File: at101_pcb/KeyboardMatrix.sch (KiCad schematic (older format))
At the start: 229 parts, among them SW1.1 KEY_ESCAPE, SW1.10 KEY_F9, SW1.11 KEY_F10, SW1.12 KEY_F11, SW1.13 KEY_F12, SW1.14 KEY_PRINTSCREEN, SW1.15 KEY_SCROLL_LOCK, SW1.16 KEY_PAUSE, SW1.2 KEY_F1, SW1.3 KEY_F2, SW1.4 KEY_F3, SW1.5 KEY_F4, SW1.6 KEY_F5, SW1.7 KEY_F6, SW1.8 KEY_F7, SW1.9 KEY_F8, SW2.1 KEY_BACKQUOTE, SW2.10 KEY_9, SW2.11 KEY_0, SW2.12 KEY_MINUS, SW2.13 KEY_EQUALS, SW2.14 KEY_BACKSPACE, SW2.15 KEY_INSERT, SW2.16 KEY_HOME, SW2.17 KEY_PGUP, SW2.18 KEY_NUMLOCK, SW2.19 KEY_NUMDIVIDE, SW2.2 KEY_1, SW2.20 KEY_NUMTIMES, SW2.21 KEY_NUMMINUS, SW2.3 KEY_2, SW2.4 KEY_3, SW2.5 KEY_4, SW2.6 KEY_5, SW2.7 KEY_6, SW2.8 KEY_7, SW2.9 KEY_8, SW3.1 KEY_TAB, SW3.10 KEY_O, SW3.11 KEY_P, SW3.12 KEY_LEFTBRACKET, SW3.13 KEY_RIGHTBRACKET, SW3.14 KEY_ANSIBACKSLASH, SW3.15 KEY_DELETE, SW3.16 KEY_END, SW3.17 KEY_PGDN, SW3.18 KEY_NUM7, SW3.19 KEY_NUM8, SW3.2 KEY_Q, SW3.20 KEY_NUM9, SW3.21 KEY_NUMPLUS, SW3.3 KEY_W, SW3.4 KEY_E, SW3.5 KEY_R, SW3.6 KEY_T, SW3.7 KEY_Y, SW3.8 KEY_U, SW3.9 KEY_I, SW3B.1 KEY_NUMBIGPLUS, SW4.1 KEY_CAPSLOCK, SW4.10 KEY_L, SW4.11 KEY_SEMICOLON, SW4.12 KEY_QUOTE, SW4.13 KEY_ISOBACKSLASH, SW4.14 KEY_ISOENTER, SW4.15 KEY_ENTER, SW4.16 KEY_NUM4, SW4.17 KEY_NUM5, SW4.18 KEY_NUM6, SW4.19 KEY_NUMEQUALS, SW4.2 KEY_A, SW4.3 KEY_S, SW4.4 KEY_D, SW4.5 KEY_F, SW4.6 KEY_G, SW4.7 KEY_H, SW4.8 KEY_J, SW4.9 KEY_K, SW4.B1 KEY_CAPSLOCK_1.5, SW4C.1 KEY_CAPSLOCK_1.25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

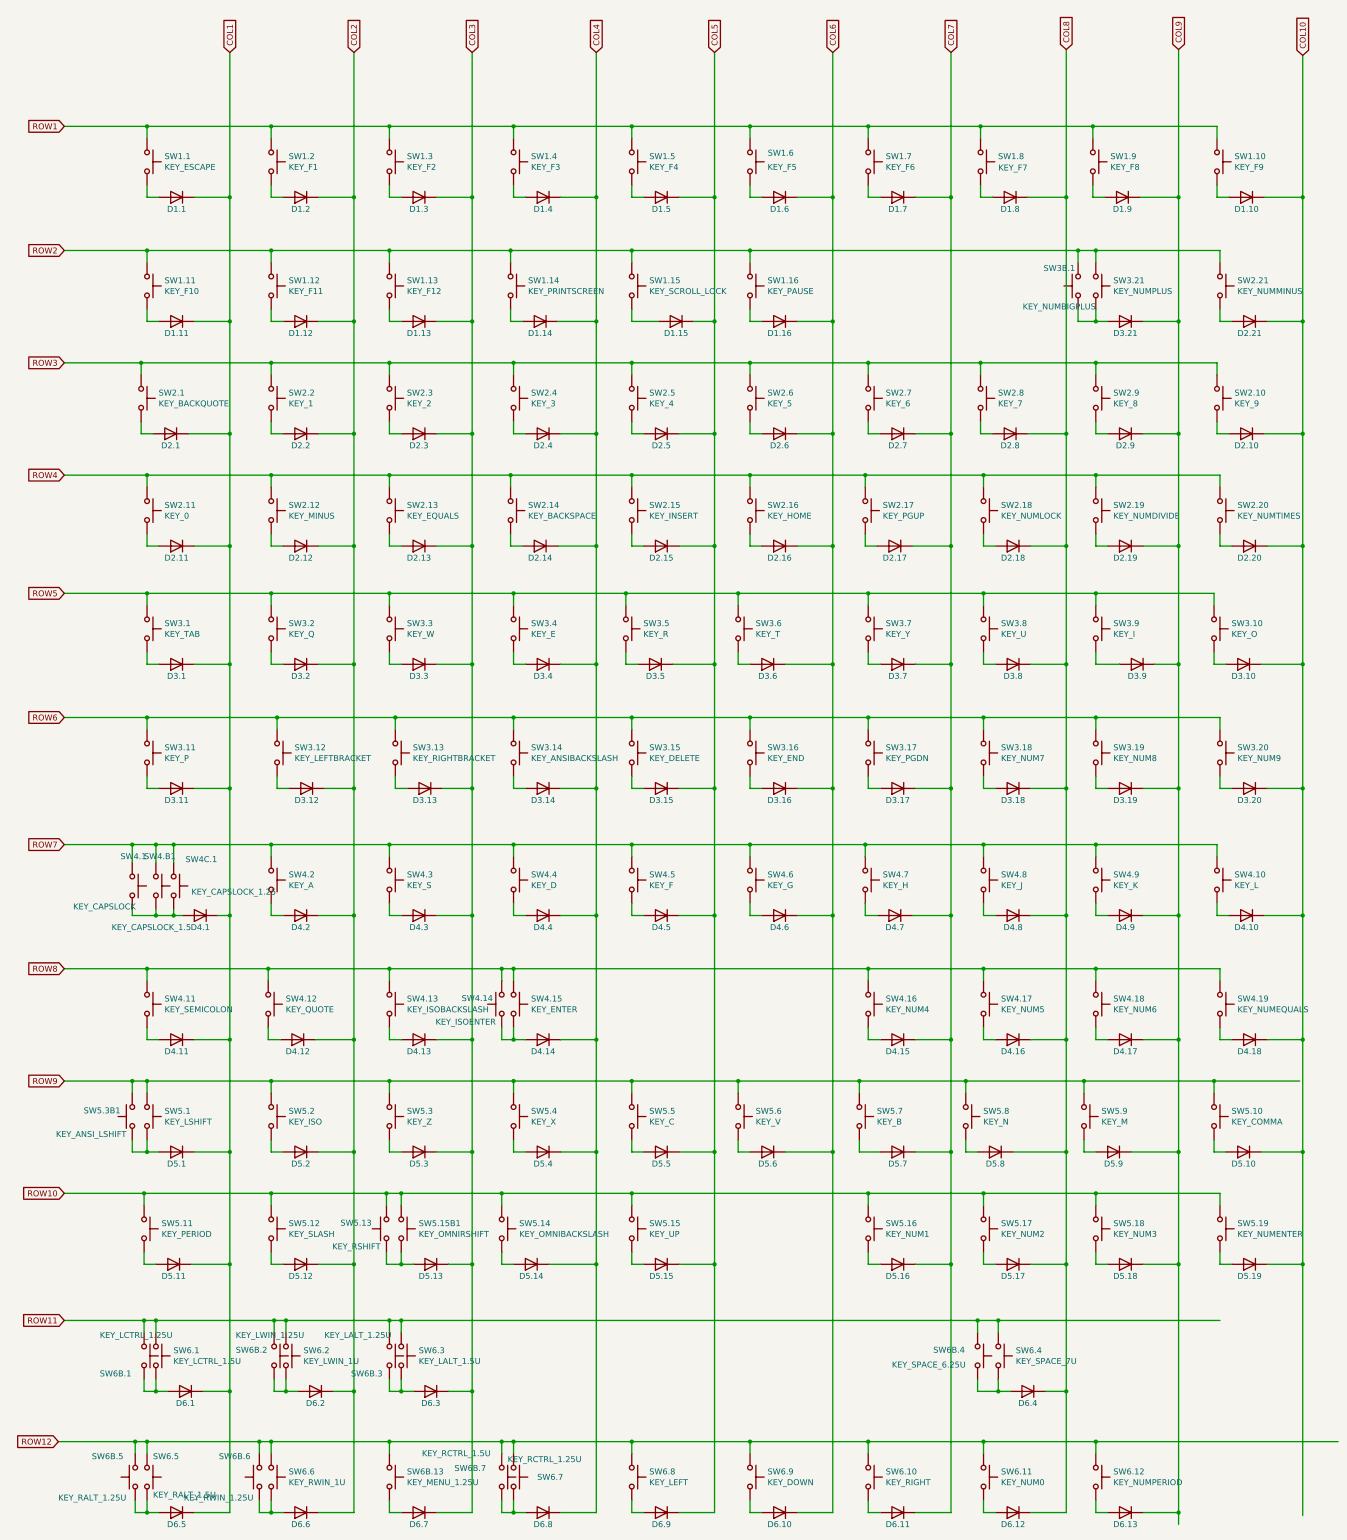
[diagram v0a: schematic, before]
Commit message: Correct AT10[12]W? switch labels
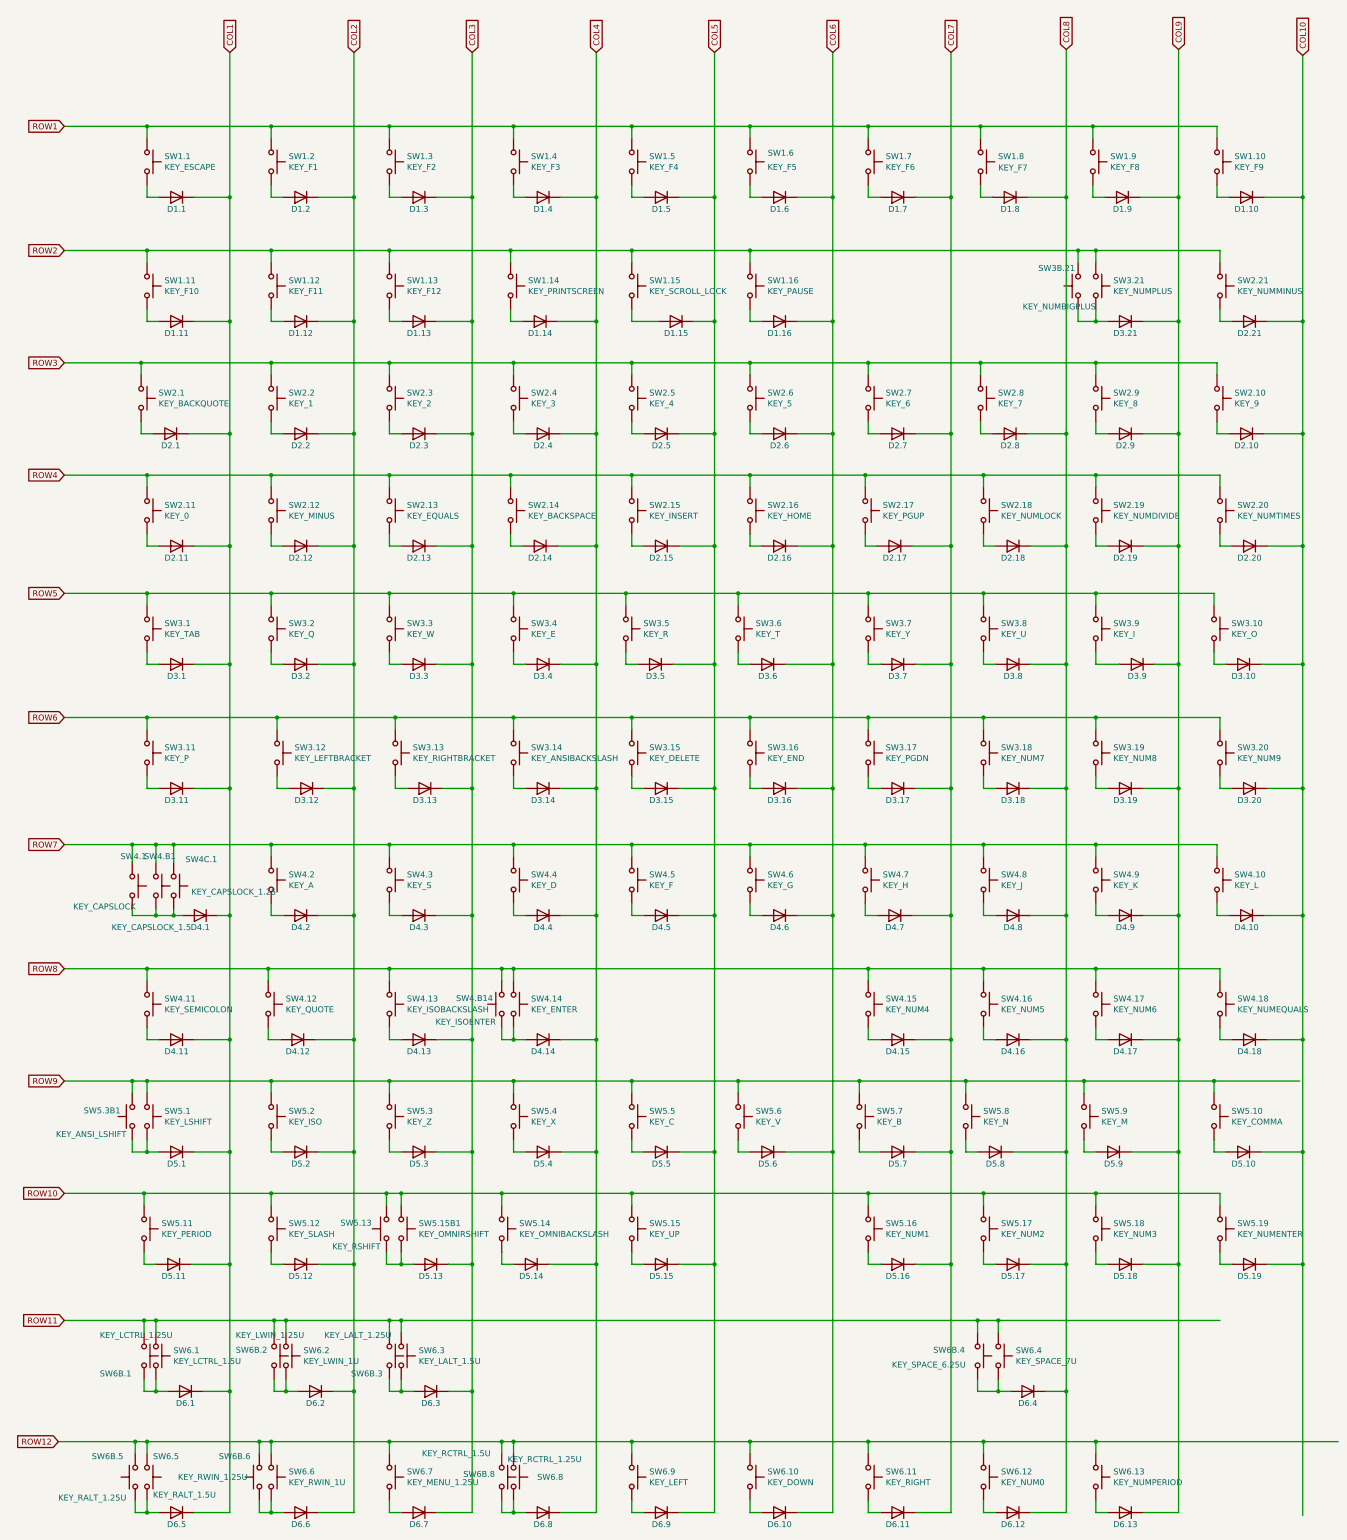
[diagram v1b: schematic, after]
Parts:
- renumbered SW3B.1 to SW3B.21, SW4.15 to SW4.14, SW4.16 to SW4.15, SW4.17 to SW4.16, SW4.18 to SW4.17, SW4.19 to SW4.18, SW4.14 to SW4.B14, SW6.9 to SW6.10, SW6.10 to SW6.11, SW6.11 to SW6.12, SW6.12 to SW6.13, SW6B.13 to SW6.7, SW6.7 to SW6.8, SW6.8 to SW6.9, SW6B.7 to SW6B.8
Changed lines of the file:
@@
 	17075 10350 17275 10350
 $Comp
-L Switch:SW_Push SW4.16
+L Switch:SW_Push SW4.15
 U 1 1 5D151639
 P 15150 13225
-F 0 "SW4.16" V 15104 13373 50  0000 L CNN
+F 0 "SW4.15" V 15104 13373 50  0000 L CNN
 F 1 "KEY_NUM4" V 15195 13373 50  0000 L CNN
 F 2 "MX_Alps_Hybrid:MX-1U-NoLED" H 15150 13425 50  0001 C CNN
@@
 	10100 11975 10100 11875
 $Comp
-L Switch:SW_Push SW4.17
+L Switch:SW_Push SW4.16
 U 1 1 5D151718
 P 16125 13225
-F 0 "SW4.17" V 16079 13373 50  0000 L CNN
+F 0 "SW4.16" V 16079 13373 50  0000 L CNN
 F 1 "KEY_NUM5" V 16170 13373 50  0000 L CNN
 F 2 "MX_Alps_Hybrid:MX-1U-NoLED" H 16125 13425 50  0001 C CNN
@@
 	11100 11975 11100 11875
 $Comp
-L Switch:SW_Push SW4.18
+L Switch:SW_Push SW4.17
 U 1 1 5D1517E5
 P 17075 13225
-F 0 "SW4.18" V 17029 13373 50  0000 L CNN
+F 0 "SW4.17" V 17029 13373 50  0000 L CNN
 F 1 "KEY_NUM6" V 17120 13373 50  0000 L CNN
 F 2 "MX_Alps_Hybrid:MX-1U-NoLED" H 17075 13425 50  0001 C CNN
@@
 	14150 8400 14250 8400
 $Comp
-L Switch:SW_Push SW4.15
+L Switch:SW_Push SW4.14
 U 1 1 5D151A5B
 P 12150 13225
-F 0 "SW4.15" V 12104 13373 50  0000 L CNN
+F 0 "SW4.14" V 12104 13373 50  0000 L CNN
 F 1 "KEY_ENTER" V 12195 13373 50  0000 L CNN
 F 2 "MX_Alps_Hybrid:MX-Big-Ass-Enter-NoLED" H 12150 13425 50  0001 C CNN
@@
 $EndComp
 $Comp
-L Switch:SW_Push SW6.12
+L Switch:SW_Push SW6.13
 U 1 1 5D1519FF
 P 17075 17225
-F 0 "SW6.12" V 17029 17373 50  0000 L CNN
+F 0 "SW6.13" V 17029 17373 50  0000 L CNN
 F 1 "KEY_NUMPERIOD" V 17120 17373 50  0000 L CNN
 F 2 "MX_Alps_Hybrid:MX-1U-NoLED" H 17075 17425 50  0001 C CNN
@@
 $EndComp
 $Comp
-L Switch:SW_Push SW6.7
+L Switch:SW_Push SW6.8
 U 1 1 5D1515B0
 P 12150 17225
-F 0 "SW6.7" V 12150 17425 50  0000 L CNN
+F 0 "SW6.8" V 12150 17425 50  0000 L CNN
 F 1 "KEY_RCTRL_1.5U" V 11950 16450 50  0000 L CNN
 F 2 "MX_Alps_Hybrid:MX-1.5U-NoLED" H 12150 17425 50  0001 C CNN
@@
 $EndComp
 $Comp
-L Switch:SW_Push SW4.19
+L Switch:SW_Push SW4.18
 U 1 1 5D90919A
 P 18125 13225
-F 0 "SW4.19" V 18079 13373 50  0000 L CNN
+F 0 "SW4.18" V 18079 13373 50  0000 L CNN
 F 1 "KEY_NUMEQUALS" V 18170 13373 50  0000 L CNN
 F 2 "MX_Alps_Hybrid:MX-1U-NoLED" H 18125 13425 50  0001 C CNN
@@
 P 10000 17225
 F 0 "SW6B.6" V 10175 17300 50  0000 L CNN
-F 1 "KEY_RWIN_1.25U" V 9825 17275 50  0000 L CNN
+F 1 "KEY_RWIN_1.25U" V 10000 17325 50  0000 L CNN
 F 2 "MX_Alps_Hybrid:MX-1.25U-NoLED" H 10000 17425 50  0001 C CNN
 F 3 "" H 10000 17425 50  0001 C CNN
@@
 Connection ~ 11200 16500
 $Comp
-L Switch:SW_Push SW4.14
+L Switch:SW_Push SW4.B14
 U 1 1 5CC64DE3
 P 12050 13225
-F 0 "SW4.14" V 12100 13300 50  0000 L CNN
+F 0 "SW4.B14" V 12100 13300 50  0000 L CNN
 F 1 "KEY_ISOENTER" V 11900 13275 50  0000 L CNN
 F 2 "MX_Alps_Hybrid:MX-ISO-ReversedStabilizers-NoLED" H 12050 13425 50  0001 C CNN
@@
 Wire Wire Line
 	12050 17025 12050 16925
-$Comp
-L Switch:SW_Push SW6B.7
-U 1 1 5DDA1B4D
-P 12050 17225
-F 0 "SW6B.7" V 11975 16825 50  0000 L CNN
-F 1 "KEY_RCTRL_1.25U" V 11900 17275 50  0000 L CNN
-F 2 "MX_Alps_Hybrid:MX-1.25U-NoLED" H 12050 17425 50  0001 C CNN
-F 3 "" H 12050 17425 50  0001 C CNN
-	1    12050 17225
-	0    1    1    0
-$EndComp
 Wire Wire Line
 	9050 9850 9050 9750
@@
 $EndComp
 $Comp
-L Switch:SW_Push SW6.8
+L Switch:SW_Push SW6.9
 U 1 1 5D15168E
 P 13150 17225
-F 0 "SW6.8" V 13104 17373 50  0000 L CNN
+F 0 "SW6.9" V 13104 17373 50  0000 L CNN
 F 1 "KEY_LEFT" V 13195 17373 50  0000 L CNN
 F 2 "MX_Alps_Hybrid:MX-1U-NoLED" H 13150 17425 50  0001 C CNN
@@
 	14150 17025 14150 16925
 $Comp
-L Switch:SW_Push SW6.9
+L Switch:SW_Push SW6.10
 U 1 1 5D15175B
 P 14150 17225
-F 0 "SW6.9" V 14104 17373 50  0000 L CNN
+F 0 "SW6.10" V 14104 17373 50  0000 L CNN
 F 1 "KEY_DOWN" V 14195 17373 50  0000 L CNN
 F 2 "MX_Alps_Hybrid:MX-1U-NoLED" H 14150 17425 50  0001 C CNN
@@
 $EndComp
 $Comp
-L Switch:SW_Push SW6.10
+L Switch:SW_Push SW6.11
 U 1 1 5D151851
 P 15150 17225
-F 0 "SW6.10" V 15104 17373 50  0000 L CNN
+F 0 "SW6.11" V 15104 17373 50  0000 L CNN
 F 1 "KEY_RIGHT" V 15195 17373 50  0000 L CNN
 F 2 "MX_Alps_Hybrid:MX-1U-NoLED" H 15150 17425 50  0001 C CNN
@@
 $EndComp
 $Comp
-L Switch:SW_Push SW6.11
+L Switch:SW_Push SW6.12
 U 1 1 5D151921
 P 16125 17225
-F 0 "SW6.11" V 16079 17373 50  0000 L CNN
+F 0 "SW6.12" V 16079 17373 50  0000 L CNN
 F 1 "KEY_NUM0" V 16170 17373 50  0000 L CNN
 F 2 "MX_Alps_Hybrid:MX-2U-ReversedStabilizers-NoLED" H 16125 17425 50  0001 C CNN
@@
 Connection ~ 18825 15425
 Connection ~ 17075 16925
-Connection ~ 17775 17525
-Wire Wire Line
-	17775 17525 17775 17625
 Wire Wire Line
 	13150 17025 13150 16925
@@
 $EndComp
 $Comp
-L Switch:SW_Push SW3B.1
+L Switch:SW_Push SW3B.21
 U 1 1 5CFE7A00
 P 16925 7150
-F 0 "SW3B.1" V 17075 7175 50  0000 L CNN
+F 0 "SW3B.21" V 17075 7175 50  0000 L CNN
 F 1 "KEY_NUMBIGPLUS" V 16750 7000 50  0000 L CNN
 F 2 "MX_Alps_Hybrid:MX-2U-NoLED" H 16925 7350 50  0001 C CNN
@@
 Wire Wire Line
 	17075 16925 19125 16925
-$Comp
-L Switch:SW_Push SW6B.13
-U 1 1 5DCF57FE
-P 11100 17225
-F 0 "SW6B.13" V 11054 17373 50  0000 L CNN
-F 1 "KEY_MENU_1.25U" V 11145 17373 50  0000 L CNN
-F 2 "MX_Alps_Hybrid:MX-1.25U-NoLED" H 11100 17425 50  0001 C CNN
-F 3 "" H 11100 17425 50  0001 C CNN
-	1    11100 17225
-	0    1    1    0
-$EndComp
 Wire Wire Line
 	17775 6400 17775 7450
@@
 Wire Wire Line
 	18825 7450 18825 8400
+$Comp
+L Switch:SW_Push SW6B.8
+U 1 1 5DDA1B4D
+P 12050 17225
+F 0 "SW6B.8" V 12025 16900 50  0000 L CNN
+F 1 "KEY_RCTRL_1.25U" V 11900 17275 50  0000 L CNN
+F 2 "MX_Alps_Hybrid:MX-1.25U-NoLED" H 12050 17425 50  0001 C CNN
+F 3 "" H 12050 17425 50  0001 C CNN
+	1    12050 17225
+	0    1    1    0
+$EndComp
+$Comp
+L Switch:SW_Push SW6.7
+U 1 1 5DCF57FE
+P 11100 17225
+F 0 "SW6.7" V 11054 17373 50  0000 L CNN
+F 1 "KEY_MENU_1.25U" V 11145 17373 50  0000 L CNN
+F 2 "MX_Alps_Hybrid:MX-1.25U-NoLED" H 11100 17425 50  0001 C CNN
+F 3 "" H 11100 17425 50  0001 C CNN
+	1    11100 17225
+	0    1    1    0
+$EndComp
 $EndSCHEMATC
